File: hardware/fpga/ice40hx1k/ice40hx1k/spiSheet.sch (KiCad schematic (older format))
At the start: 9 parts, among them J2 Conn_02x05_Odd_Even, U5 AT25SF081-SSHD-X

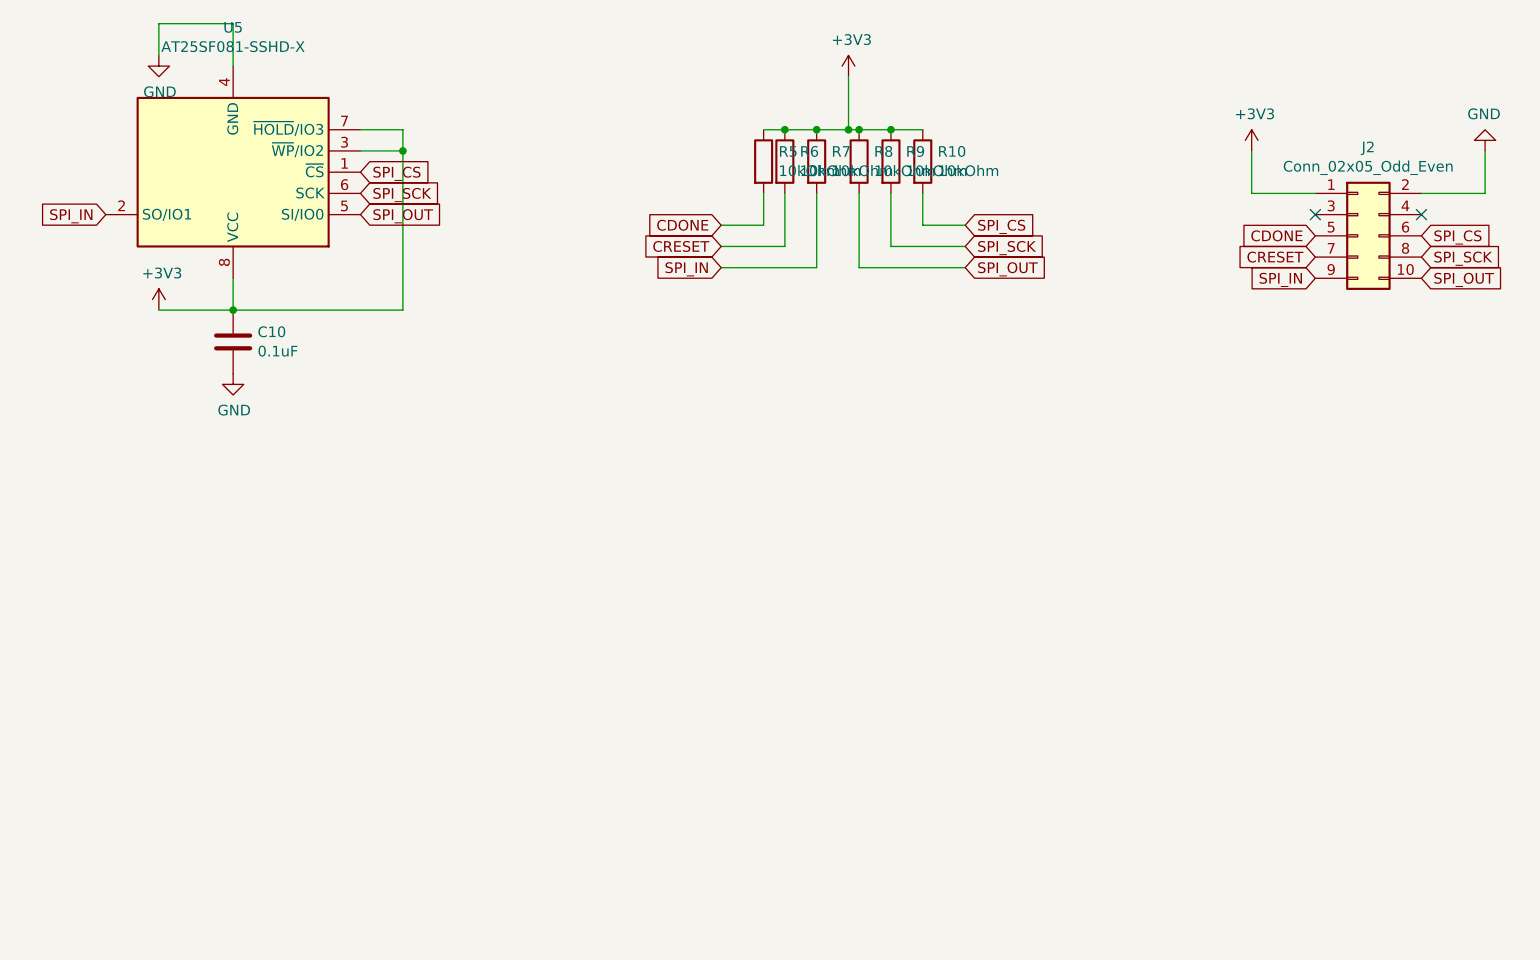
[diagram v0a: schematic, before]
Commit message: std FPGA skeleton
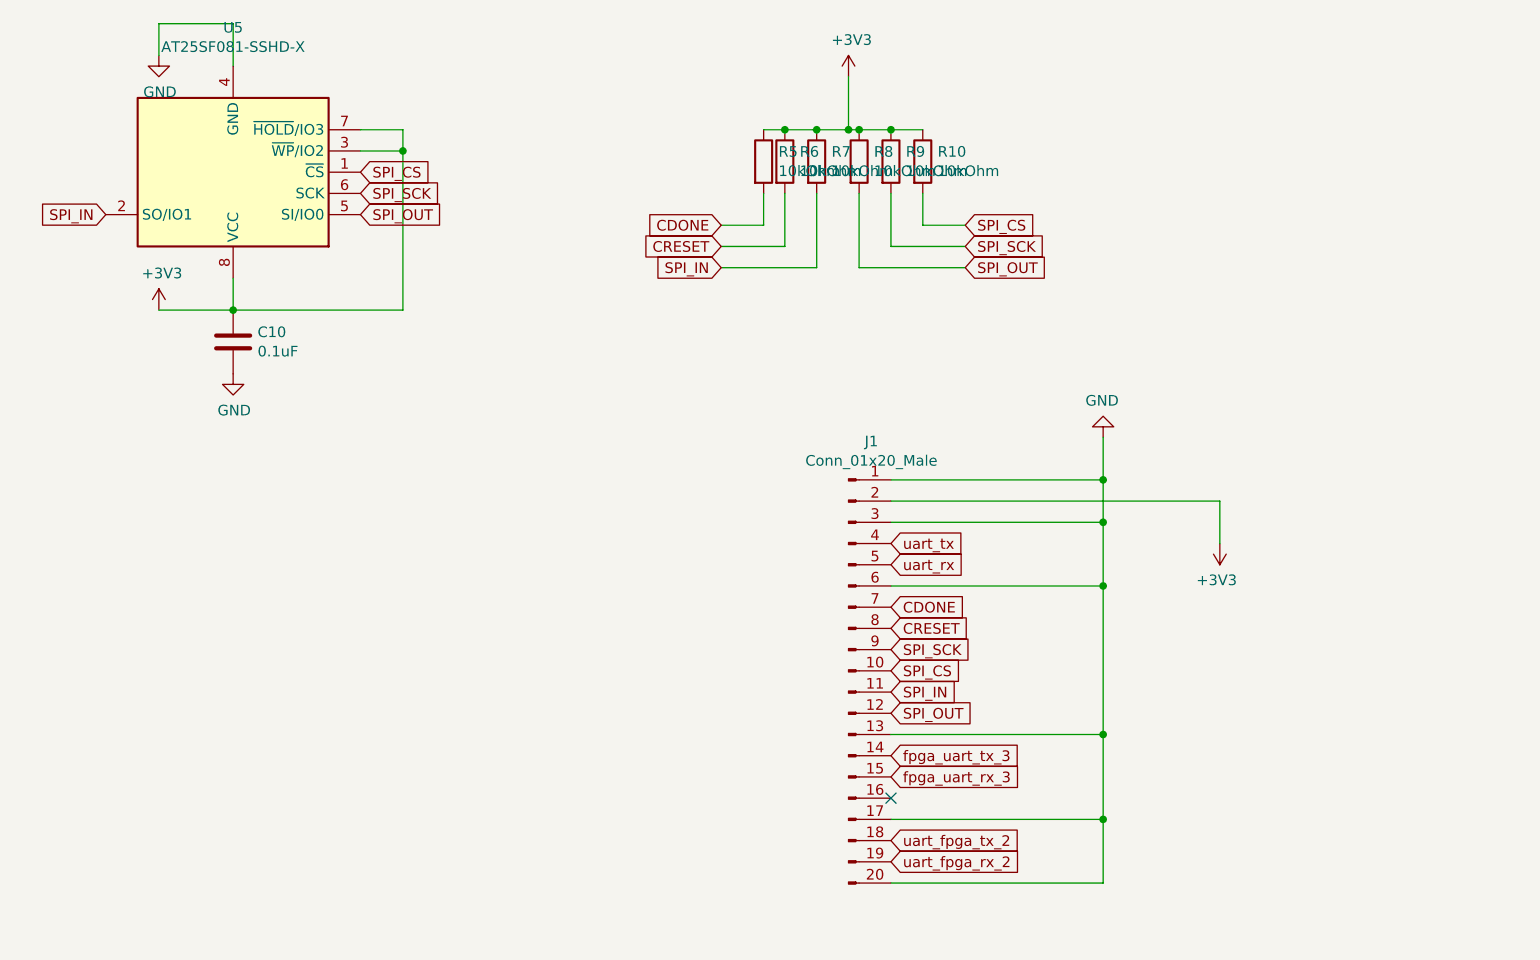
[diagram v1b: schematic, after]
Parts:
- removed J2: Conn_02x05_Odd_Even, Connector_PinHeader_2.54mm:PinHeader_2x05_P2.54mm_Vertical, symbol Connector_Generic:Conn_02x05_Odd_Even
- added J1: Conn_01x20_Male, Connector_PinHeader_2.54mm:PinHeader_1x20_P2.54mm_Vertical, symbol Connector:Conn_01x20_Male
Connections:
- net +3V3: now also J1.2 (Pin_2)
- net CDONE: now also J1.7 (Pin_7)
- net CRESET: now also J1.8 (Pin_8)
- net GND: now also J1.1 (Pin_1), J1.13 (Pin_13), J1.17 (Pin_17), J1.20 (Pin_20), J1.3 (Pin_3), J1.6 (Pin_6)
- net SPI_CS: now also J1.10 (Pin_10)
- net SPI_IN: now also J1.11 (Pin_11)
- net SPI_OUT: now also J1.12 (Pin_12)
- net SPI_SCK: now also J1.9 (Pin_9)
- new net fpga_uart_rx_3: J1.15 (Pin_15)
- new net fpga_uart_tx_3: J1.14 (Pin_14)
- new net uart_fpga_rx_2: J1.19 (Pin_19)
- new net uart_fpga_tx_2: J1.18 (Pin_18)
- new net uart_rx: J1.5 (Pin_5)
- new net uart_tx: J1.4 (Pin_4)
- no-connect marks 2 -> 1
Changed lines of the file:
@@
 AR Path="/5E610BE8" Ref="U?"  Part="1"
 AR Path="/5E5F2441/5E610BE8" Ref="U5"  Part="1"
+AR Path="/5E9ED365/5E610BE8" Ref="U5"  Part="1"
 F 0 "U5" H 2300 1219 50  0000 C CNN
 F 1 "AT25SF081-SSHD-X" H 2300 1310 50  0000 C CNN
@@
 AR Path="/5E610BEE" Ref="C?"  Part="1"
 AR Path="/5E5F2441/5E610BEE" Ref="C10"  Part="1"
+AR Path="/5E9ED365/5E610BEE" Ref="C10"  Part="1"
 F 0 "C10" H 2415 2746 50  0000 L CNN
 F 1 "0.1uF" H 2415 2655 50  0000 L CNN
@@
 AR Path="/5E610BF4" Ref="#PWR?"  Part="1"
 AR Path="/5E5F2441/5E610BF4" Ref="#PWR013"  Part="1"
+AR Path="/5E9ED365/5E610BF4" Ref="#PWR013"  Part="1"
 F 0 "#PWR013" H 1950 2400 50  0001 C CNN
 F 1 "+3V3" H 1965 2723 50  0000 C CNN
@@
 AR Path="/5E610C07" Ref="#PWR?"  Part="1"
 AR Path="/5E5F2441/5E610C07" Ref="#PWR014"  Part="1"
+AR Path="/5E9ED365/5E610C07" Ref="#PWR014"  Part="1"
 F 0 "#PWR014" H 2300 2600 50  0001 C CNN
 F 1 "GND" H 2305 2677 50  0000 C CNN
@@
 AR Path="/5E610C0D" Ref="#PWR?"  Part="1"
 AR Path="/5E5F2441/5E610C0D" Ref="#PWR012"  Part="1"
+AR Path="/5E9ED365/5E610C0D" Ref="#PWR012"  Part="1"
 F 0 "#PWR012" H 1950 1100 50  0001 C CNN
 F 1 "GND" H 1955 1177 50  0000 C CNN
@@
 AR Path="/5E62B581" Ref="R?"  Part="1"
 AR Path="/5E5F2441/5E62B581" Ref="R7"  Part="1"
+AR Path="/5E9ED365/5E62B581" Ref="R7"  Part="1"
 F 0 "R7" H 5120 1896 50  0000 L CNN
 F 1 "10kOhm" H 5120 1805 50  0000 L CNN
@@
 AR Path="/5E62B587" Ref="R?"  Part="1"
 AR Path="/5E5F2441/5E62B587" Ref="R8"  Part="1"
+AR Path="/5E9ED365/5E62B587" Ref="R8"  Part="1"
 F 0 "R8" H 5320 1896 50  0000 L CNN
 F 1 "10kOhm" H 5320 1805 50  0000 L CNN
@@
 AR Path="/5E62B58D" Ref="R?"  Part="1"
 AR Path="/5E5F2441/5E62B58D" Ref="R9"  Part="1"
+AR Path="/5E9ED365/5E62B58D" Ref="R9"  Part="1"
 F 0 "R9" H 5470 1896 50  0000 L CNN
 F 1 "10kOhm" H 5470 1805 50  0000 L CNN
@@
 AR Path="/5E62B593" Ref="R?"  Part="1"
 AR Path="/5E5F2441/5E62B593" Ref="R10"  Part="1"
+AR Path="/5E9ED365/5E62B593" Ref="R10"  Part="1"
 F 0 "R10" H 5620 1896 50  0000 L CNN
 F 1 "10kOhm" H 5620 1805 50  0000 L CNN
@@
 AR Path="/5E62B599" Ref="R?"  Part="1"
 AR Path="/5E5F2441/5E62B599" Ref="R5"  Part="1"
+AR Path="/5E9ED365/5E62B599" Ref="R5"  Part="1"
 F 0 "R5" H 4870 1896 50  0000 L CNN
 F 1 "10kOhm" H 4870 1805 50  0000 L CNN
@@
 AR Path="/5E62B59F" Ref="R?"  Part="1"
 AR Path="/5E5F2441/5E62B59F" Ref="R6"  Part="1"
+AR Path="/5E9ED365/5E62B59F" Ref="R6"  Part="1"
 F 0 "R6" H 4970 1896 50  0000 L CNN
 F 1 "10kOhm" H 4970 1805 50  0000 L CNN
@@
 AR Path="/5E62B5AB" Ref="#PWR?"  Part="1"
 AR Path="/5E5F2441/5E62B5AB" Ref="#PWR015"  Part="1"
+AR Path="/5E9ED365/5E62B5AB" Ref="#PWR015"  Part="1"
 F 0 "#PWR015" H 5200 1300 50  0001 C CNN
 F 1 "+3V3" H 5215 1623 50  0000 C CNN
@@
 Wire Wire Line
 	5550 2150 5750 2150
-$Comp
-L Connector_Generic:Conn_02x05_Odd_Even J2
-U 1 1 5E63A010
-P 7600 2200
-F 0 "J2" H 7650 2617 50  0000 C CNN
-F 1 "Conn_02x05_Odd_Even" H 7650 2526 50  0000 C CNN
-F 2 "Connector_PinHeader_2.54mm:PinHeader_2x05_P2.54mm_Vertical" H 7600 2200 50  0001 C CNN
-F 3 "~" H 7600 2200 50  0001 C CNN
-	1    7600 2200
-	1    0    0    -1
-$EndComp
-Text GLabel 7900 2400 2    50   Input ~ 0
+Text GLabel 5400 4450 2    50   Input ~ 0
 SPI_OUT
-Text GLabel 7900 2300 2    50   Input ~ 0
+Text GLabel 5400 4150 2    50   Input ~ 0
 SPI_SCK
-Text GLabel 7900 2200 2    50   Input ~ 0
+Text GLabel 5400 4250 2    50   Input ~ 0
 SPI_CS
-Text GLabel 7400 2400 0    50   Input ~ 0
+Text GLabel 5400 4350 2    50   Input ~ 0
 SPI_IN
-Text GLabel 7400 2200 0    50   Input ~ 0
+Text GLabel 5400 3950 2    50   Input ~ 0
 CDONE
-Text GLabel 7400 2300 0    50   Input ~ 0
+Text GLabel 5400 4050 2    50   Input ~ 0
 CRESET
 $Comp
 L power:+3V3 #PWR016
 U 1 1 5E63A01C
-P 7100 1800
-F 0 "#PWR016" H 7100 1650 50  0001 C CNN
-F 1 "+3V3" H 7115 1973 50  0000 C CNN
-F 2 "" H 7100 1800 50  0001 C CNN
-F 3 "" H 7100 1800 50  0001 C CNN
-	1    7100 1800
-	1    0    0    -1
+P 6950 3650
+F 0 "#PWR016" H 6950 3500 50  0001 C CNN
+F 1 "+3V3" H 6965 3823 50  0000 C CNN
+F 2 "" H 6950 3650 50  0001 C CNN
+F 3 "" H 6950 3650 50  0001 C CNN
+	1    6950 3650
+	-1   0    0    1
 $EndComp
 $Comp
 L power:GND #PWR017
 U 1 1 5E63A022
-P 8200 1800
-F 0 "#PWR017" H 8200 1550 50  0001 C CNN
-F 1 "GND" H 8205 1627 50  0000 C CNN
-F 2 "" H 8200 1800 50  0001 C CNN
-F 3 "" H 8200 1800 50  0001 C CNN
-	1    8200 1800
+P 6400 3150
+F 0 "#PWR017" H 6400 2900 50  0001 C CNN
+F 1 "GND" H 6405 2977 50  0000 C CNN
+F 2 "" H 6400 3150 50  0001 C CNN
+F 3 "" H 6400 3150 50  0001 C CNN
+	1    6400 3150
 	-1   0    0    1
 $EndComp
 Wire Wire Line
-	7900 2000 8200 2000
-Wire Wire Line
-	8200 2000 8200 1800
-Wire Wire Line
-	7100 1800 7100 2000
-Wire Wire Line
-	7100 2000 7400 2000
-NoConn ~ 7900 2100
-NoConn ~ 7400 2100
+	6400 3350 6400 3150
+Wire Wire Line
+	6950 3650 6950 3450
+$Comp
+L Connector:Conn_01x20_Male J1
+U 1 1 5EA4F382
+P 5200 4250
+F 0 "J1" H 5308 5331 50  0000 C CNN
+F 1 "Conn_01x20_Male" H 5308 5240 50  0000 C CNN
+F 2 "Connector_PinHeader_2.54mm:PinHeader_1x20_P2.54mm_Vertical" H 5200 4250 50  0001 C CNN
+F 3 "~" H 5200 4250 50  0001 C CNN
+	1    5200 4250
+	1    0    0    -1
+$EndComp
+Wire Wire Line
+	5400 3350 6400 3350
+Wire Wire Line
+	6400 3350 6400 3550
+Wire Wire Line
+	6400 3550 5400 3550
+Connection ~ 6400 3350
+Wire Wire Line
+	5400 5250 6400 5250
+Wire Wire Line
+	6400 5250 6400 4950
+Connection ~ 6400 3550
+Wire Wire Line
+	5400 4950 6400 4950
+Connection ~ 6400 4950
+Wire Wire Line
+	6400 4950 6400 4550
+Wire Wire Line
+	5400 4550 6400 4550
+Connection ~ 6400 4550
+Wire Wire Line
+	6400 4550 6400 3850
+Wire Wire Line
+	5400 3850 6400 3850
+Connection ~ 6400 3850
+Wire Wire Line
+	6400 3850 6400 3550
+Wire Wire Line
+	5400 3450 6950 3450
+Text GLabel 5400 3650 2    50   Input ~ 0
+uart_tx
+Text GLabel 5400 3750 2    50   Input ~ 0
+uart_rx
+Text GLabel 5400 4750 2    50   Input ~ 0
+fpga_uart_rx_3
+Text GLabel 5400 4650 2    50   Input ~ 0
+fpga_uart_tx_3
+NoConn ~ 5400 4850
+Text GLabel 5400 5050 2    50   Input ~ 0
+uart_fpga_tx_2
+Text GLabel 5400 5150 2    50   Input ~ 0
+uart_fpga_rx_2
 $EndSCHEMATC

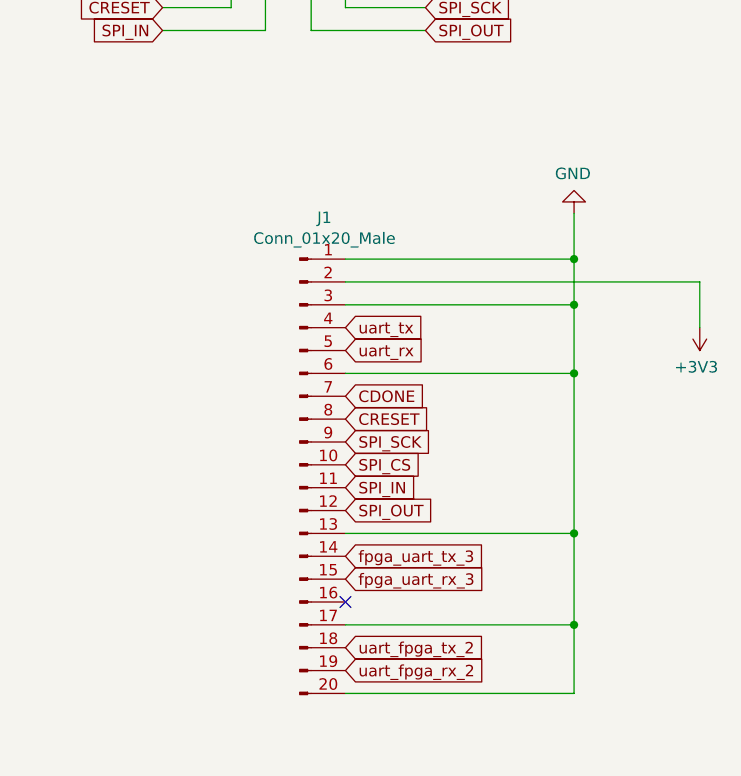
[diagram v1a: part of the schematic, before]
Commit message: std FPGA skeleton
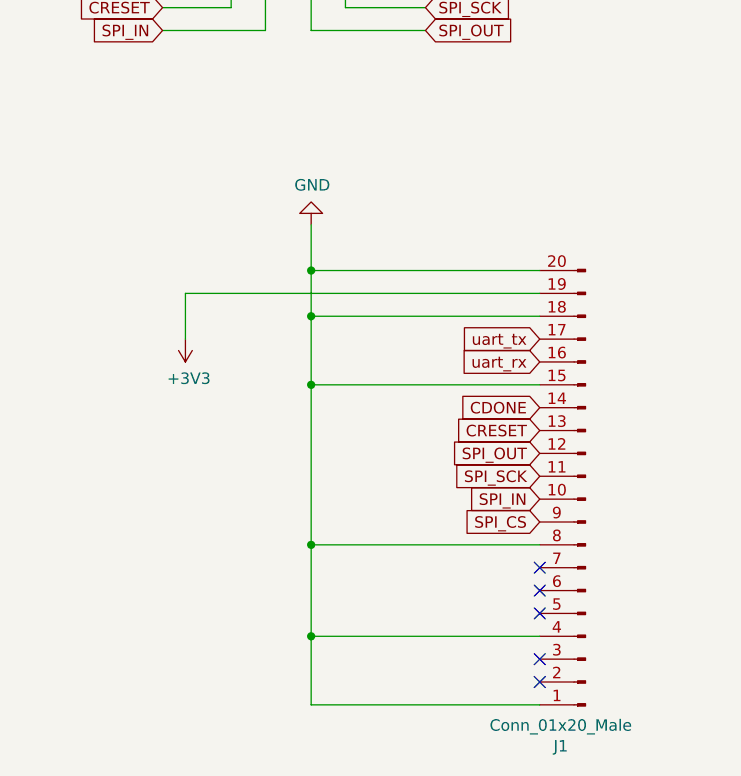
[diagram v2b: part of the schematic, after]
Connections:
- net fpga_uart_rx_3 is gone; now on net GND: J1.15 (Pin_15)
- net fpga_uart_tx_3 is gone; now on net CDONE: J1.14 (Pin_14)
- net uart_fpga_rx_2 is gone; now on net +3V3: J1.19 (Pin_19)
- net uart_fpga_tx_2 is gone; now on net GND: J1.18 (Pin_18)
- net +3V3: no longer J1.2 (Pin_2)
- net CDONE: no longer J1.7 (Pin_7)
- net CRESET: now also J1.13 (Pin_13); no longer J1.8 (Pin_8)
- net GND: now also J1.4 (Pin_4), J1.8 (Pin_8); no longer J1.13 (Pin_13), J1.17 (Pin_17), J1.3 (Pin_3), J1.6 (Pin_6)
- net SPI_CS: now also J1.9 (Pin_9); no longer J1.10 (Pin_10)
- net SPI_IN: now also J1.10 (Pin_10); no longer J1.11 (Pin_11)
- net SPI_SCK: now also J1.11 (Pin_11); no longer J1.9 (Pin_9)
- net uart_rx: now also J1.16 (Pin_16); no longer J1.5 (Pin_5)
- net uart_tx: now also J1.17 (Pin_17); no longer J1.4 (Pin_4)
- no-connect marks 1 -> 5
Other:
- moved on the sheet: J1
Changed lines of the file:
@@
 Wire Wire Line
 	5550 2150 5750 2150
-Text GLabel 5400 4450 2    50   Input ~ 0
+Text GLabel 6250 4200 0    50   Input ~ 0
 SPI_OUT
-Text GLabel 5400 4150 2    50   Input ~ 0
+Text GLabel 6250 4300 0    50   Input ~ 0
 SPI_SCK
-Text GLabel 5400 4250 2    50   Input ~ 0
+Text GLabel 6250 4500 0    50   Input ~ 0
 SPI_CS
-Text GLabel 5400 4350 2    50   Input ~ 0
+Text GLabel 6250 4400 0    50   Input ~ 0
 SPI_IN
-Text GLabel 5400 3950 2    50   Input ~ 0
+Text GLabel 6250 4000 0    50   Input ~ 0
 CDONE
-Text GLabel 5400 4050 2    50   Input ~ 0
+Text GLabel 6250 4100 0    50   Input ~ 0
 CRESET
 $Comp
 L power:+3V3 #PWR016
 U 1 1 5E63A01C
-P 6950 3650
-F 0 "#PWR016" H 6950 3500 50  0001 C CNN
-F 1 "+3V3" H 6965 3823 50  0000 C CNN
-F 2 "" H 6950 3650 50  0001 C CNN
-F 3 "" H 6950 3650 50  0001 C CNN
-	1    6950 3650
-	-1   0    0    1
+P 4700 3700
+F 0 "#PWR016" H 4700 3550 50  0001 C CNN
+F 1 "+3V3" H 4715 3873 50  0000 C CNN
+F 2 "" H 4700 3700 50  0001 C CNN
+F 3 "" H 4700 3700 50  0001 C CNN
+	1    4700 3700
+	1    0    0    1
 $EndComp
 $Comp
 L power:GND #PWR017
 U 1 1 5E63A022
-P 6400 3150
-F 0 "#PWR017" H 6400 2900 50  0001 C CNN
-F 1 "GND" H 6405 2977 50  0000 C CNN
-F 2 "" H 6400 3150 50  0001 C CNN
-F 3 "" H 6400 3150 50  0001 C CNN
-	1    6400 3150
-	-1   0    0    1
+P 5250 3200
+F 0 "#PWR017" H 5250 2950 50  0001 C CNN
+F 1 "GND" H 5255 3027 50  0000 C CNN
+F 2 "" H 5250 3200 50  0001 C CNN
+F 3 "" H 5250 3200 50  0001 C CNN
+	1    5250 3200
+	1    0    0    1
 $EndComp
 Wire Wire Line
-	6400 3350 6400 3150
+	5250 3400 5250 3200
 Wire Wire Line
-	6950 3650 6950 3450
+	4700 3700 4700 3500
+Wire Wire Line
+	6250 3400 5250 3400
+Wire Wire Line
+	5250 3400 5250 3600
+Wire Wire Line
+	5250 3600 6250 3600
+Connection ~ 5250 3400
+Wire Wire Line
+	6250 5300 5250 5300
+Wire Wire Line
+	5250 5300 5250 5000
+Connection ~ 5250 3600
+Wire Wire Line
+	6250 5000 5250 5000
+Connection ~ 5250 5000
+Wire Wire Line
+	5250 5000 5250 4600
+Wire Wire Line
+	6250 4600 5250 4600
+Connection ~ 5250 4600
+Wire Wire Line
+	5250 4600 5250 3900
+Wire Wire Line
+	6250 3900 5250 3900
+Connection ~ 5250 3900
+Wire Wire Line
+	5250 3900 5250 3600
+Wire Wire Line
+	6250 3500 4700 3500
+Text GLabel 6250 3700 0    50   Input ~ 0
+uart_tx
+Text GLabel 6250 3800 0    50   Input ~ 0
+uart_rx
+NoConn ~ 6250 4900
 $Comp
 L Connector:Conn_01x20_Male J1
 U 1 1 5EA4F382
-P 5200 4250
-F 0 "J1" H 5308 5331 50  0000 C CNN
-F 1 "Conn_01x20_Male" H 5308 5240 50  0000 C CNN
-F 2 "Connector_PinHeader_2.54mm:PinHeader_1x20_P2.54mm_Vertical" H 5200 4250 50  0001 C CNN
-F 3 "~" H 5200 4250 50  0001 C CNN
-	1    5200 4250
-	1    0    0    -1
+P 6450 4400
+F 0 "J1" H 6558 5481 50  0000 C CNN
+F 1 "Conn_01x20_Male" H 6558 5390 50  0000 C CNN
+F 2 "Connector_PinHeader_2.54mm:PinHeader_1x20_P2.54mm_Vertical" H 6450 4400 50  0001 C CNN
+F 3 "~" H 6450 4400 50  0001 C CNN
+	1    6450 4400
+	-1   0    0    1
 $EndComp
-Wire Wire Line
-	5400 3350 6400 3350
-Wire Wire Line
-	6400 3350 6400 3550
-Wire Wire Line
-	6400 3550 5400 3550
-Connection ~ 6400 3350
-Wire Wire Line
-	5400 5250 6400 5250
-Wire Wire Line
-	6400 5250 6400 4950
-Connection ~ 6400 3550
-Wire Wire Line
-	5400 4950 6400 4950
-Connection ~ 6400 4950
-Wire Wire Line
-	6400 4950 6400 4550
-Wire Wire Line
-	5400 4550 6400 4550
-Connection ~ 6400 4550
-Wire Wire Line
-	6400 4550 6400 3850
-Wire Wire Line
-	5400 3850 6400 3850
-Connection ~ 6400 3850
-Wire Wire Line
-	6400 3850 6400 3550
-Wire Wire Line
-	5400 3450 6950 3450
-Text GLabel 5400 3650 2    50   Input ~ 0
-uart_tx
-Text GLabel 5400 3750 2    50   Input ~ 0
-uart_rx
-Text GLabel 5400 4750 2    50   Input ~ 0
-fpga_uart_rx_3
-Text GLabel 5400 4650 2    50   Input ~ 0
-fpga_uart_tx_3
-NoConn ~ 5400 4850
-Text GLabel 5400 5050 2    50   Input ~ 0
-uart_fpga_tx_2
-Text GLabel 5400 5150 2    50   Input ~ 0
-uart_fpga_rx_2
+NoConn ~ 6250 4700
+NoConn ~ 6250 4800
+NoConn ~ 6250 5100
+NoConn ~ 6250 5200
 $EndSCHEMATC
